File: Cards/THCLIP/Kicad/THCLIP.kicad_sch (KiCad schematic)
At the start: 11 parts, among them J2 Conn_01x03_Pin, J3 Conn_01x05_Pin, U1 RS3K-2424S/H3

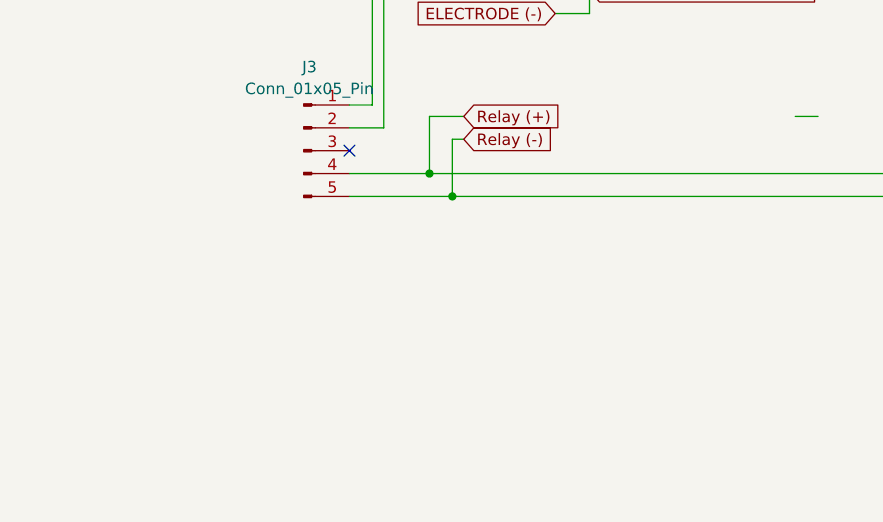
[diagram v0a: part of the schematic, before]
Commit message: Added selection criteria for relay in Schematics
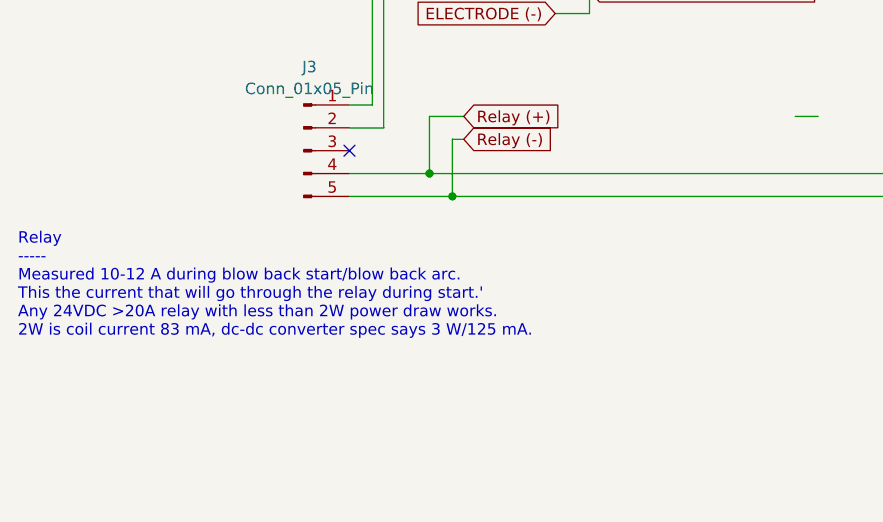
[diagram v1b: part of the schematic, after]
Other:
- note added: "Relay ----- Measured 10-12 A during blow back start/blow back arc. This the current that will go through the relay during start.' Any 24VDC >20A relay with less than 2W power draw works. 2W is coil current 83 mA, dc-dc converter spec says 3 W/125 mA."
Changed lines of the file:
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@@
+		)
+	)
+	(text "Relay\n-----\nMeasured 10-12 A during blow back start/blow back arc.\nThis the current that will go through the relay during start.'\nAny 24VDC >20A relay with less than 2W power draw works.\n2W is coil current 83 mA, dc-dc converter spec says 3 W/125 mA."
+		(exclude_from_sim no)
+		(at 22.86 83.566 0)
+		(effects
+			(font
+				(size 1.27 1.27)
+			)
+			(justify left)
 		)
 	)

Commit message: THCLIP released
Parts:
- added K1: Relay_SPDT, symbol Relay:Relay_SPDT
- R1: value 10k -> 100k
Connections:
- net WORK PIECE GND (+): now also K1.30
- net +24V UNREG renamed 24V UNREG +
- net 24V UNREG +: now also K1.86
- net -24V UNREG renamed 24V UNREG GND
- net 24V UNREG GND: now also K1.85, K1.87a
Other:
- note added: "E7000 Recieve input height sensing signal Activate dc-dc converter - 24V DC will appear on the dc-dc converter output - 0.24 mA will flow through via 100 kOhm resistor (shorted output) - Relay will activate - Connection between work piece ground and torch shield ground is broken - Output will be unshorted, current through resistor stops flowing - 23V voltage appears between electrode and work pie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"
- note added: "FY0022 connector 8-9 Torch shield safety 1+4 Torch ground"
- note added: "Relay ----- Measured 10-12 A during blow back start/blow back arc. This the current that will go through the relay during start. No current flows during plasma cutting. Any 24VDC >20A relay with less than 2W power draw works. 2W is coil current 83 mA, dc-dc converter spec says 3 W/125 mA."
- note added: "To machine"
- note added: "To torch"
- note added: "Torch connector"
- note removed: "E7000 Recieve input height sensing signal Activate relay to break workpiece and torch shield ground This activates 24VDC sensing voltage between electrode and work piece ground (1 mA) When Arc voltage > x V: send contact Signal (repeat signal x times?) exit sensing mode After x msecs: exit sensing mode Loss of height sensing signal: exit sensing mode Exit of sensing mode: disable height sensings 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"
- note removed: "Relay ----- Measured 10-12 A during blow back start/blow back arc. This the current that will go through the relay during start.' Any 24VDC >20A relay with less than 2W power draw works. 2W is coil current 83 mA, dc-dc converter spec says 3 W/125 mA."
- moved on the sheet: D1, H1, H2, H3, H4, J2, J3, R1, R4, R5, U1

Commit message: Cleaned schematics
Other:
- note added: "DC-DC converter --------------- Recom Power RS3K-2424S/H3 Isolated dc-dc converter with on/off signal"
- note added: "FY0022 + FY0023 connector (central adaptor) 8 and 9 Torch shield safety 1+4 Torch ground"
- note added: "Process ------- Recieve input height sensing signal Activate dc-dc converter - 24V DC will appear on the dc-dc converter output - A small current will flow through via 100 kOhm resistor (shorted output) - Relay will activate - Connection between work piece ground and torch shield ground is broken - Output will be unshorted, current through resistor stops flowing - 23V voltage appears between elec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"
- note added: "To machine (plasma cutter)"
- note removed: "E7000 Recieve input height sensing signal Activate dc-dc converter - 24V DC will appear on the dc-dc converter output - 0.24 mA will flow through via 100 kOhm resistor (shorted output) - Relay will activate - Connection between work piece ground and torch shield ground is broken - Output will be unshorted, current through resistor stops flowing - 23V voltage appears between electrode and work pie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"
- note removed: "FY0022 connector 8-9 Torch shield safety 1+4 Torch ground"
- note removed: "To machine"
- note removed: "Torch connector"
- moved on the sheet: D1, H1, H2, H3, H4, J2, J3, K1, R1, R4, R5, U1
